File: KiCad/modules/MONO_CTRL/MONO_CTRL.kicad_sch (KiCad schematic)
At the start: 51 parts, among them J1 Conn_01x01_Pin, J11 Conn_01x01_Pin, J12 Conn_01x01_Pin, J13 Conn_01x01_Pin, J14 Conn_01x01_Pin, J15 Conn_01x01_Pin, J16 Conn_01x01_Pin, J17 Conn_01x01_Pin, J18 Conn_01x01_Pin, J19 Conn_01x01_Pin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

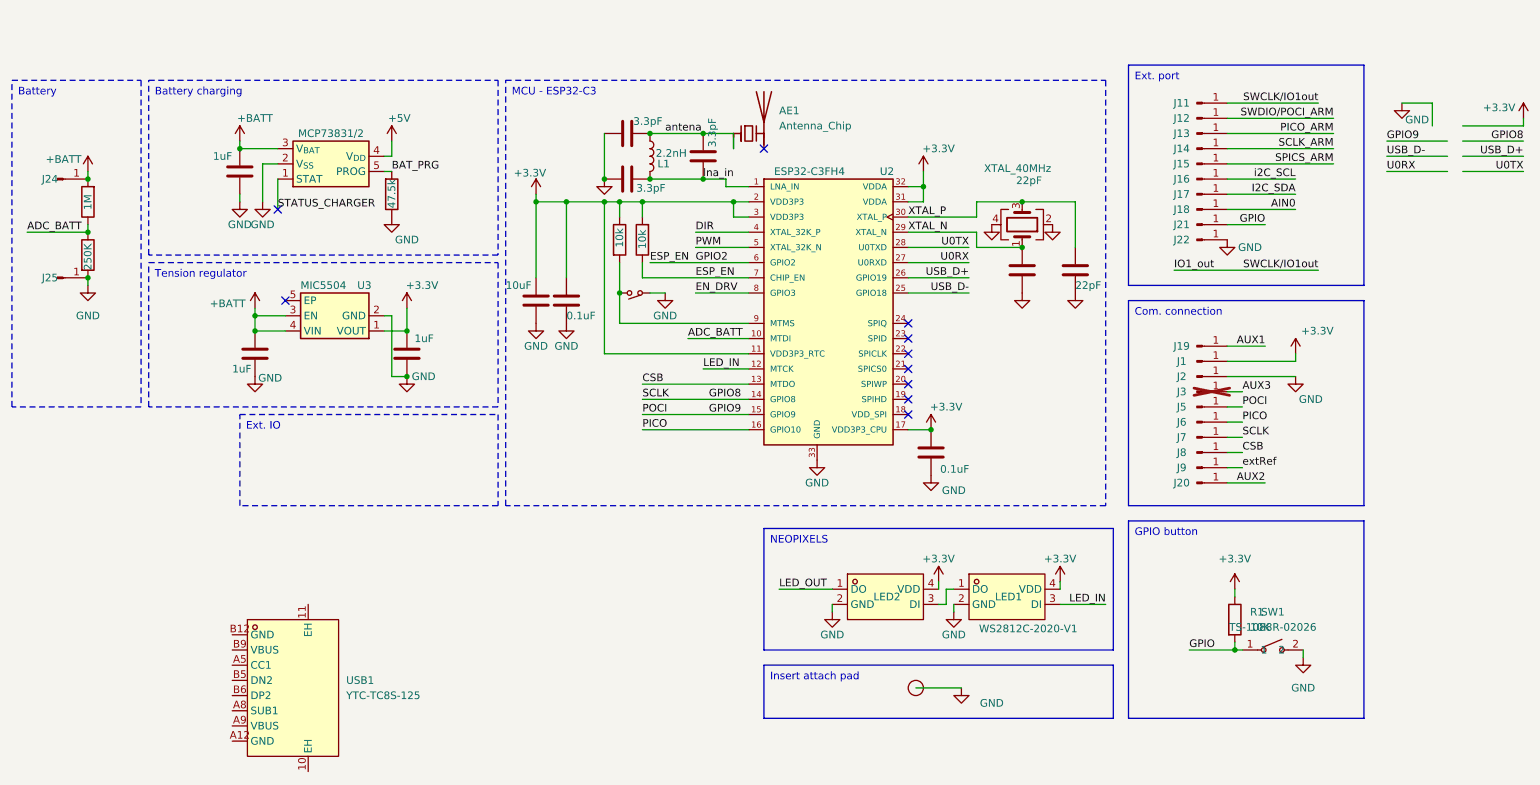
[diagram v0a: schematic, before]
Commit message: finished mono moudule, should be ready for manufacture
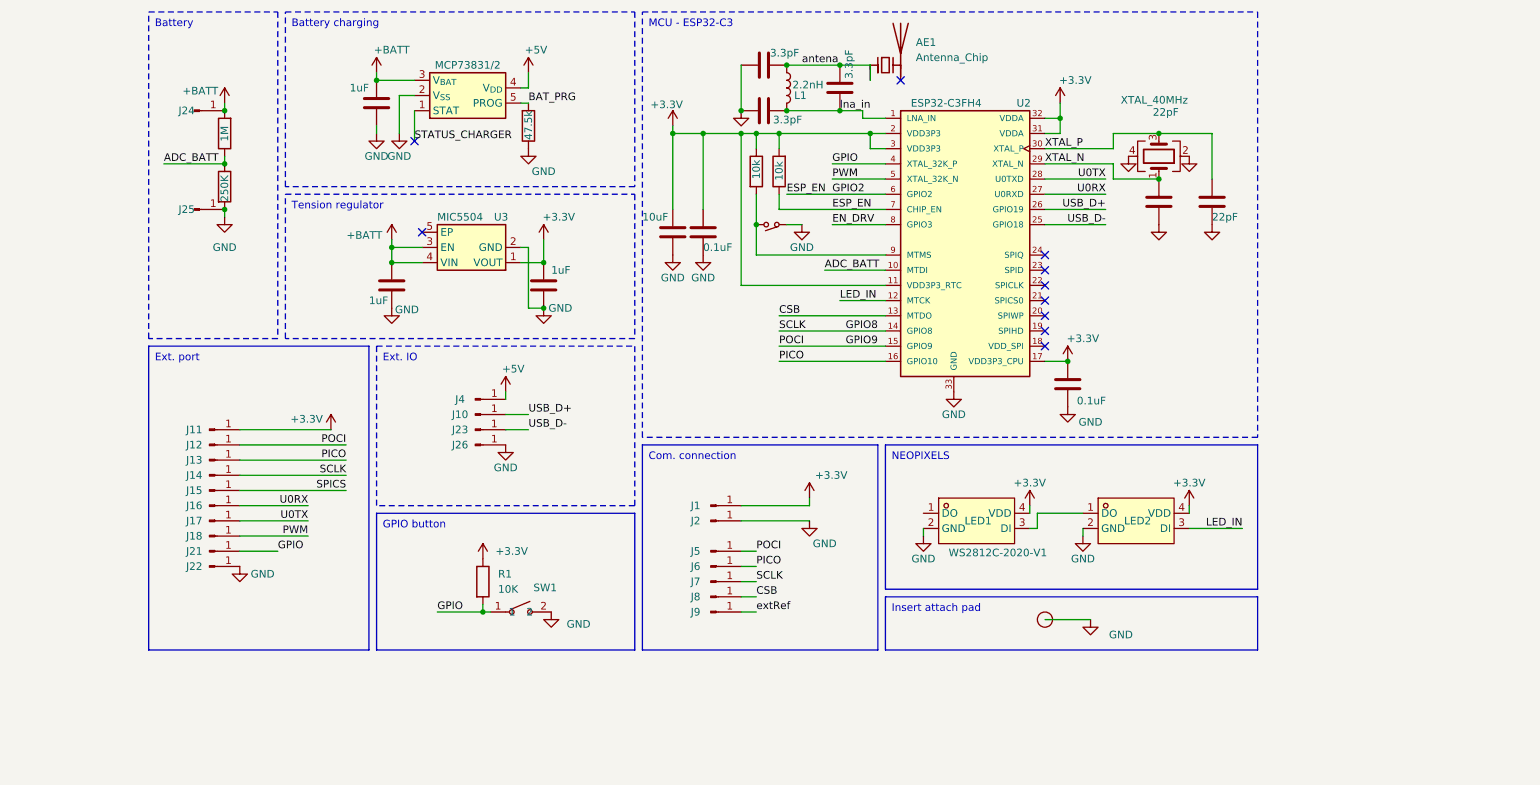
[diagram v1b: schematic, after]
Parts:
- removed J19, J20, J3: Conn_01x01_Pin, Connector_PinHeader_1.27mm:PinHeader_1x01_P1.27mm_Vertical, symbol Connector:Conn_01x01_Pin
- removed USB1: YTC-TC8S-125, 00_lcsc:USB-C-SMD_YIYUAN_YTC-TC8S-125, symbol 00_lcsc:YTC-TC8S-125
- added J10, J23, J26, J4: Conn_01x01_Pin, Connector_PinHeader_1.27mm:PinHeader_1x01_P1.27mm_Vertical, symbol Connector:Conn_01x01_Pin
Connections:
- net AIN0 is gone; now on net PWM: J18.1 (Pin_1)
- net DIR is gone; now on net GPIO: U2.4 (XTAL_32K_P)
- net I2C_SDA is gone; now on net U0TX: J17.1 (Pin_1)
- net IO1_out is gone; now on net +3.3V: J11.1 (Pin_1)
- net PICO_ARM is gone; now on net PICO: J13.1 (Pin_1)
- net SCLK_ARM is gone; now on net GPIO8: J14.1 (Pin_1)
- net SWDIO/POCI_ARM is gone; now on net GPIO9: J12.1 (Pin_1)
- net i2C_SCL is gone; now on net U0RX: J16.1 (Pin_1)
- net +5V: now also J4.1 (Pin_1)
- net GND: now also J26.1 (Pin_1)
- net LED_IN: now also LED2.3 (DI); no longer LED1.3 (DI)
- net USB_D+: now also J10.1 (Pin_1)
- net USB_D-: now also J23.1 (Pin_1)
- net at LED1.1 (DO): no longer LED2.3 (DI)
- net LED_OUT: no longer names the net of LED2.1 (DO)
- net LED_OUT: now also LED1.3 (DI)
- net SPICS_ARM renamed SPICS
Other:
- title: Communication Module -> Communication Mono
- moved on the sheet: AE1, J1, J11, J12, J13, J14, J15, J16, J17, J18, J2, J21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

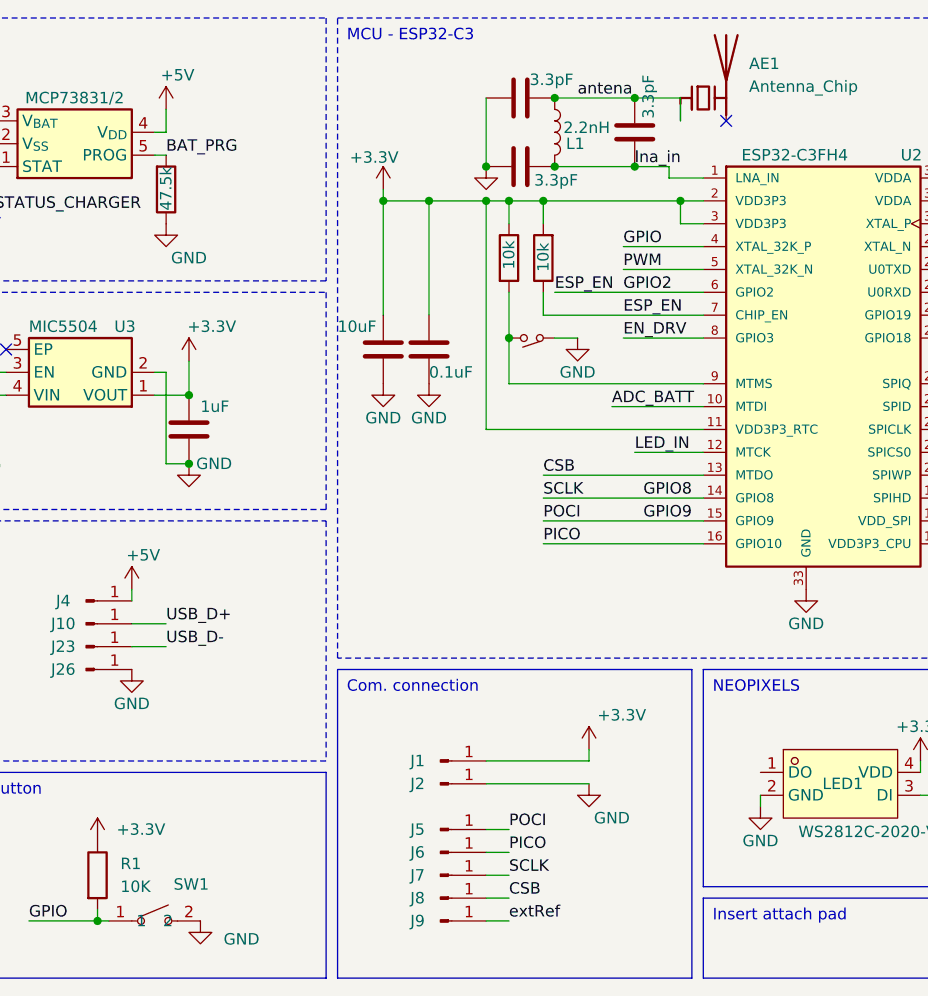
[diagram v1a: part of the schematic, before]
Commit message: fixed MONOCOM ERC and DRC: via size, missing pins
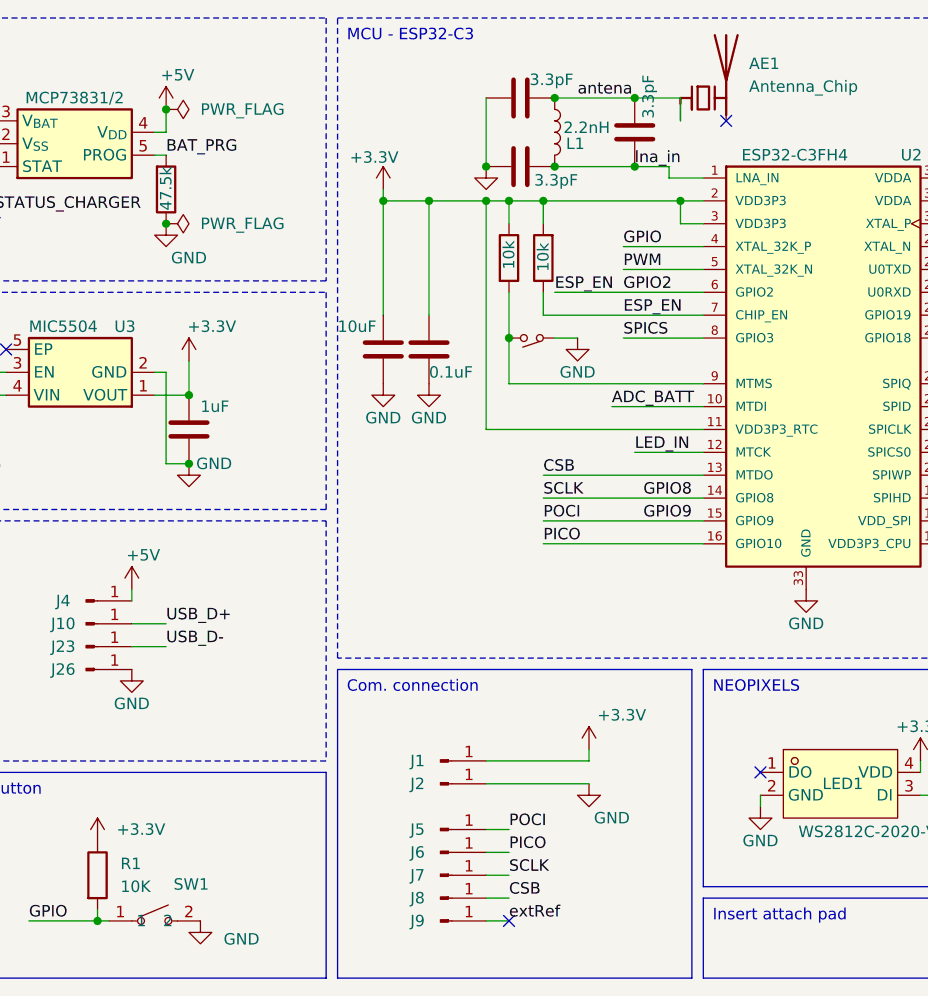
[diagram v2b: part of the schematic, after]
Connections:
- net EN_DRV is gone; now on net SPICS: U2.8 (GPIO3)
- no-connect marks 10 -> 12
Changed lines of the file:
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@@
 	)
 	(junction
+		(at 116.84 57.15)
+		(diameter 0)
+		(color 0 0 0 0)
+	)
+	(junction
 		(at 158.75 54.61)
 		(diameter 0)
@@
 	)
 	(junction
+		(at 116.84 44.45)
+		(diameter 0)
+		(color 0 0 0 0)
+	)
+	(junction
 		(at 160.02 50.8)
 		(diameter 0)
@@
 	)
 	(no_connect
+		(at 154.94 134.62)
+	)
+	(no_connect
 		(at 203.2 82.55)
 	)
@@
 		(at 97.79 55.88)
 	)
+	(no_connect
+		(at 182.88 118.11)
+	)
 	(wire
 		(pts
@@
 		)
 	)
+	(label "SPICS"
+		(at 167.64 69.85 0)
+		(fields_autoplaced yes)
+		(effects
+			(font
+				(size 1.27 1.27)
+			)
+			(justify left bottom)
+		)
+	)
 	(label "U0TX"
 		(at 213.36 62.23 180)
@@
 		)
 	)
-	(label "EN_DRV"
-		(at 167.64 69.85 0)
-		(fields_autoplaced yes)
-		(effects
-			(font
-				(size 1.27 1.27)
-			)
-			(justify left bottom)
-		)
-	)
 	(label "ESP_EN"
 		(at 160.02 64.77 0)
@@
 	)
 	(symbol
+		(lib_id "power:PWR_FLAG")
+		(at 116.84 57.15 270)
+		(unit 1)
+		(exclude_from_sim no)
+		(in_bom yes)
+		(on_board yes)
+		(dnp no)
+		(fields_autoplaced yes)
+		(property "Reference" "#FLG02"
+			(at 118.745 57.15 0)
+			(effects
+				(font
+					(size 1.27 1.27)
+				)
+				(hide yes)
+			)
+		)
+		(property "Value" "PWR_FLAG"
+			(at 120.65 57.1499 90)
+			(effects
+				(font
+					(size 1.27 1.27)
+				)
+				(justify left)
+			)
+		)
+		(property "Footprint" ""
+			(at 116.84 57.15 0)
+			(effects
+				(font
+					(size 1.27 1.27)
+				)
+				(hide yes)
+			)
+		)
+		(property "Datasheet" "~"
+			(at 116.84 57.15 0)
+			(effects
+				(font
+					(size 1.27 1.27)
+				)
+				(hide yes)
+			)
+		)
+		(property "Description" "Special symbol for telling ERC where power comes from"
+			(at 116.84 57.15 0)
+			(effects
+				(font
+					(size 1.27 1.27)
+				)
+				(hide yes)
+			)
+		)
+		(pin "1"
+		)
+		(instances
+			(project "MONO_CTRL"
+				(path "/c83c4528-97f7-431c-a266-0d1ca2cf363e"
+					(reference "#FLG02")
+					(unit 1)
+				)
+			)
+		)
+	)
+	(symbol
 		(lib_id "Connector:Conn_01x01_Pin")
 		(at 147.32 124.46 0)
@@
 					(unit 1)
 				)
+			)
+		)
+	)
+	(symbol
+		(lib_id "power:PWR_FLAG")
+		(at 116.84 44.45 270)
+		(unit 1)
+		(exclude_from_sim no)
+		(in_bom yes)
+		(on_board yes)
+		(dnp no)
+		(fields_autoplaced yes)
+		(property "Reference" "#FLG01"
+			(at 118.745 44.45 0)
+			(effects
+				(font
+					(size 1.27 1.27)
+				)
+				(hide yes)
+			)
+		)
+		(property "Value" "PWR_FLAG"
+			(at 120.65 44.4499 90)
+			(effects
+				(font
+					(size 1.27 1.27)
+				)
+				(justify left)
+			)
+		)
+		(property "Footprint" ""
+			(at 116.84 44.45 0)
+			(effects
+				(font
+					(size 1.27 1.27)
+				)
+				(hide yes)
+			)
+		)
+		(property "Datasheet" "~"
+			(at 116.84 44.45 0)
+			(effects
+				(font
+					(size 1.27 1.27)
+				)
+				(hide yes)
+			)
+		)
+		(property "Description" "Special symbol for telling ERC where power comes from"
+			(at 116.84 44.45 0)
+			(effects
+				(font
+					(size 1.27 1.27)
+				)
+				(hide yes)
+			)
+		)
+		(pin "1"
+		)
+		(instances
+			(project "MONO_CTRL"
+				(path "/c83c4528-97f7-431c-a266-0d1ca2cf363e"
+					(reference "#FLG01")
+					(unit 1)
+				)
